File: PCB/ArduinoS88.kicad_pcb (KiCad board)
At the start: 2 copper layers, 49.5 x 61 mm, 24 parts, among them J1 S88 Output, J2 S88 Input, J3 AVR-ISP-6, J4 Screw_Terminal_01x03, J5 Screw_Terminal_01x03, J6 Screw_Terminal_01x03, J7 Screw_Terminal_01x03, J8 Screw_Terminal_01x03, J9 Screw_Terminal_01x02, U1 ATmega8-16PU

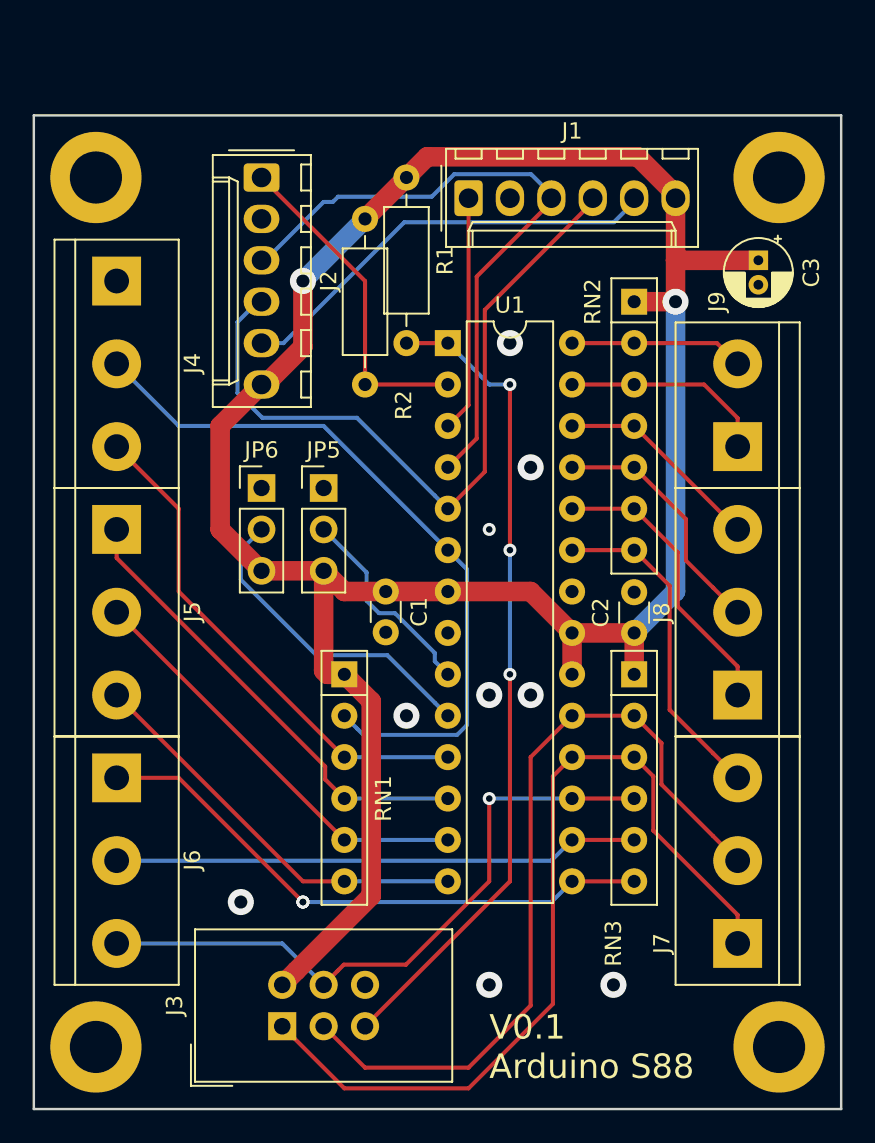
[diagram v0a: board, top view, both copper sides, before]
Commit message: Updated connectors and added Gerber files
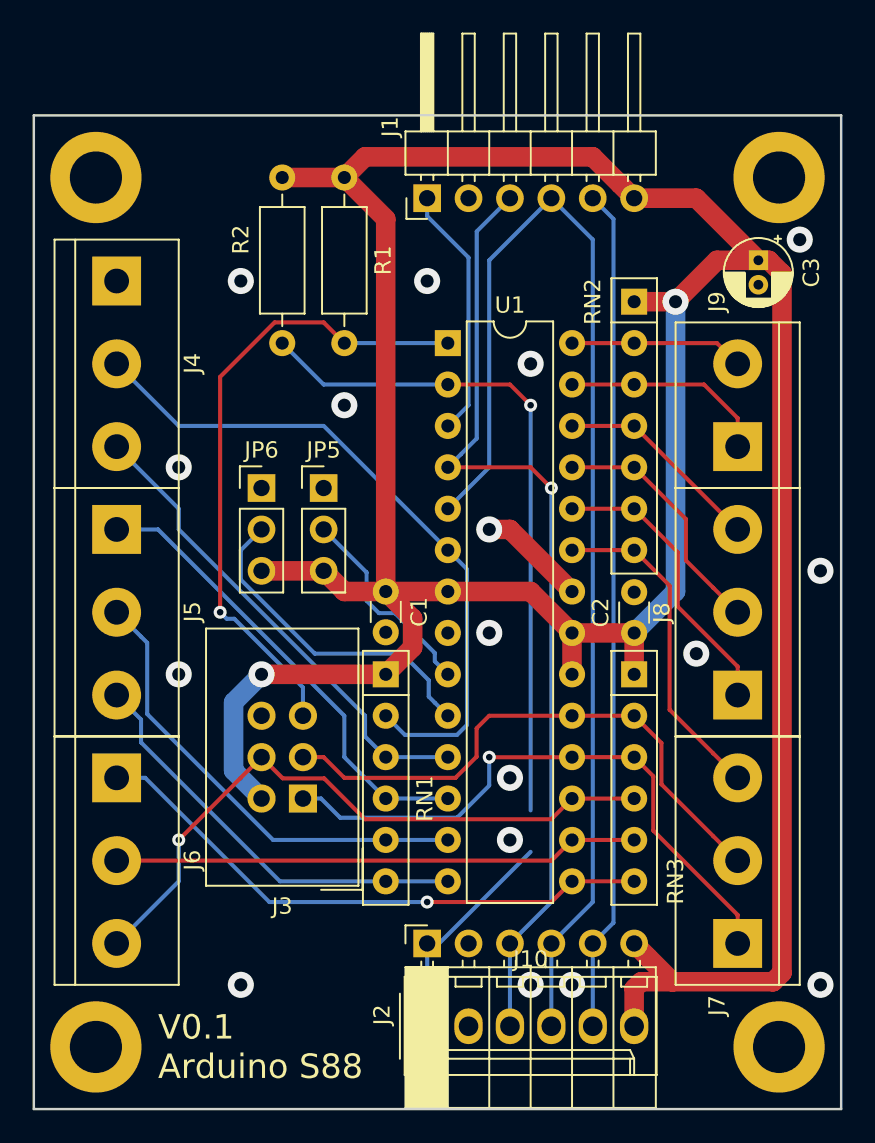
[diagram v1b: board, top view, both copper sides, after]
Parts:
- added J10: S88 Input, Connector_Molex:Molex_KK-254_AE-6410-06A_1x06_P2.54mm_Vertical, F.Cu at (94.0, 81.3)
- J1: footprint Connector_Molex:Molex_KK-254_AE-6410-06A_1x06_P2.54mm_Vertical -> Connector_PinHeader_2.54mm:PinHeader_1x06_P2.54mm_Horizontal
- J2: footprint Connector_Molex:Molex_KK-254_AE-6410-06A_1x06_P2.54mm_Vertical -> Connector_PinSocket_2.54mm:PinSocket_1x06_P2.54mm_Horizontal
- moved J2 48.1 mm to (94.0, 76.2), turned to 90 degrees
- moved J3 14.0 mm to (86.4, 67.3), turned to 180 degrees
- moved R2 5.68 mm to (85.1, 29.2)
- moved R1 3.81 mm to (88.9, 29.2)
- moved J1 2.54 mm to (94.0, 30.5), turned to 90 degrees
- moved RN1 2.54 mm to (91.4, 59.7)
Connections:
- net Net-(J1-Pad1) renamed /S88_DataOut
- net Net-(J1-Pad3) renamed /S88_CLK
- net Net-(J1-Pad4) renamed /S88_PS
- net Net-(J1-Pad5) renamed /S88_Reset
- net Net-(J2-Pad1) renamed /S88_DataIn
- net Net-(J3-Pad1) renamed /In8
- net Net-(J3-Pad3) renamed /In9
- net Net-(J3-Pad4) renamed /In7
- net Net-(J4-Pad2) renamed /In0
- net Net-(J4-Pad3) renamed /In1
- net Net-(J5-Pad1) renamed /In2
- net Net-(J5-Pad2) renamed /In3
- net Net-(J5-Pad3) renamed /In4
- net Net-(J6-Pad1) renamed /In5
- net Net-(J6-Pad2) renamed /In6
- net Net-(J7-Pad3) renamed /In10
- net Net-(J8-Pad1) renamed /In11
- net Net-(J8-Pad2) renamed /In12
- net Net-(J8-Pad3) renamed /In13
- net Net-(J9-Pad1) renamed /In14
- net Net-(J9-Pad2) renamed /In15
- net Net-(JP5-Pad2) renamed /Cfg0
- net Net-(JP6-Pad2) renamed /Cfg1
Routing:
- net VCC: track 142.6 -> 201.5 mm
- net /S88_DataIn: track 20.4 -> 55.4 mm, vias 0 -> 1
- net /S88_PS: track 44.9 -> 74.8 mm
- net /S88_Reset: track 26.9 -> 51.9 mm
- net /S88_CLK: track 39.9 -> 59.0 mm, vias 0 -> 1
- net /In8: track 53.8 -> 37.4 mm, vias 0 -> 1
- net /In9: track 49.5 -> 35.0 mm
- net Net-(J3-Pad5): track 50.5 -> 39.0 mm, vias 3 -> 1
- net GND: track 0.06 -> 6.71 mm, vias 8 -> 17
- net /In3: track 26.1 -> 28.7 mm
- net /In0: track 44.5 -> 42.0 mm
- net /In1: track 31.2 -> 29.7 mm
- net /S88_DataOut: track 14.5 -> 15.5 mm
- net /In4: track 25.1 -> 25.9 mm
- net /Cfg1: track 19.8 -> 20.4 mm
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
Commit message: Updated for manufacturing
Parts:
- moved REF** 1.27 mm to (114.3, 82.5)
- moved REF** 1.27 mm to (114.3, 29.2)
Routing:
- net VCC: track 201.5 -> 199.0 mm
- net GND: vias 17 -> 14
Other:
- board size 49.5 x 61 mm -> 48.3 x 61 mm
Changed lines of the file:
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@@
     (thickness 1.6)
     (drawings 8)
-    (tracks 232)
+    (tracks 229)
     (zones 0)
     (modules 25)
@@
     (pcbplotparams
       (layerselection 0x010f0_ffffffff)
-      (usegerberextensions false)
+      (usegerberextensions true)
       (usegerberattributes false)
       (usegerberadvancedattributes false)
@@
       (viasonmask false)
       (mode 1)
-      (useauxorigin false)
+      (useauxorigin true)
       (hpglpennumber 1)
       (hpglpenspeed 20)
@@
   )
   (module MountingHole:MountingHole_3.2mm_M3_DIN965_Pad (layer F.Cu)
-    (at 115.57 82.55)
+    (at 114.3 82.55)
     (descr "Mounting Hole 3.2mm, M3, DIN965")
     (tags "mounting hole 3.2mm m3 din965")
@@
   )
   (module MountingHole:MountingHole_3.2mm_M3_DIN965_Pad (layer F.Cu)
-    (at 115.57 29.21)
+    (at 114.3 29.21)
     (descr "Mounting Hole 3.2mm, M3, DIN965")
     (tags "mounting hole 3.2mm m3 din965")
@@
     (effects (font (size 1.5 1.5) (thickness 0.3)) (justify left))
   )
-  (target plus (at 69.85 86.36) (size 5) (width 0.15) (layer Edge.Cuts))
+  (target plus (at 87.022562 79.030951) (size 5) (width 0.15) (layer Edge.Cuts))
   (dimension 60.96 (width 0.3) (layer Dwgs.User)
     (gr_text "60,960 mm" (at 129.1 55.88 270) (layer Dwgs.User)
@@
   )
   (gr_line (start 69.85 86.36) (end 69.85 25.4) (layer Edge.Cuts) (width 0.15))
-  (gr_line (start 119.38 86.36) (end 69.85 86.36) (layer Edge.Cuts) (width 0.15))
-  (gr_line (start 119.38 25.4) (end 119.38 86.36) (layer Edge.Cuts) (width 0.15))
-  (gr_line (start 69.85 25.4) (end 119.38 25.4) (layer Edge.Cuts) (width 0.15))
-  (dimension 49.53 (width 0.3) (layer Dwgs.User)
-    (gr_text "49,530 mm" (at 94.691343 96.836647) (layer Dwgs.User)
+  (gr_line (start 118.11 86.36) (end 69.85 86.36) (layer Edge.Cuts) (width 0.15))
+  (gr_line (start 118.11 25.4) (end 118.11 86.36) (layer Edge.Cuts) (width 0.15))
+  (gr_line (start 69.85 25.4) (end 118.11 25.4) (layer Edge.Cuts) (width 0.15))
+  (dimension 48.26 (width 0.3) (layer Dwgs.User)
+    (gr_text "48,260 mm" (at 93.98 97.863353) (layer Dwgs.User)
       (effects (font (size 1.5 1.5) (thickness 0.3)))
     )
-    (feature1 (pts (xy 69.926343 88.386647) (xy 69.926343 95.323068)))
-    (feature2 (pts (xy 119.456343 88.386647) (xy 119.456343 95.323068)))
-    (crossbar (pts (xy 119.456343 94.736647) (xy 69.926343 94.736647)))
-    (arrow1a (pts (xy 69.926343 94.736647) (xy 71.052847 94.150226)))
-    (arrow1b (pts (xy 69.926343 94.736647) (xy 71.052847 95.323068)))
-    (arrow2a (pts (xy 119.456343 94.736647) (xy 118.329839 94.150226)))
-    (arrow2b (pts (xy 119.456343 94.736647) (xy 118.329839 95.323068)))
+    (feature1 (pts (xy 69.85 88.9) (xy 69.85 96.349774)))
+    (feature2 (pts (xy 118.11 88.9) (xy 118.11 96.349774)))
+    (crossbar (pts (xy 118.11 95.763353) (xy 69.85 95.763353)))
+    (arrow1a (pts (xy 69.85 95.763353) (xy 70.976504 95.176932)))
+    (arrow1b (pts (xy 69.85 95.763353) (xy 70.976504 96.349774)))
+    (arrow2a (pts (xy 118.11 95.763353) (xy 116.983496 95.176932)))
+    (arrow2b (pts (xy 118.11 95.763353) (xy 116.983496 96.349774)))
   )
   (via (at 78.74 46.99) (size 1.6) (drill 0.8) (layers F.Cu B.Cu) (net 3))
@@
   (segment (start 111.76 34.29) (end 109.22 36.83) (width 1.2) (layer F.Cu) (net 1))
   (segment (start 114.3 34.29) (end 111.76 34.29) (width 1.2) (layer F.Cu) (net 1))
-  (segment (start 110.49 30.48) (end 114.3 34.29) (width 1.2) (layer F.Cu) (net 1))
-  (segment (start 106.68 30.48) (end 110.49 30.48) (width 1.2) (layer F.Cu) (net 1))
   (segment (start 85.09 29.21) (end 88.9 29.21) (width 1.2) (layer F.Cu) (net 1))
   (segment (start 105.830001 29.630001) (end 106.68 30.48) (width 1.2) (layer F.Cu) (net 1))
@@
   (via (at 83.82 59.69) (size 1.6) (drill 0.8) (layers F.Cu B.Cu) (net 1))
   (segment (start 91.44 59.69) (end 83.82 59.69) (width 1.2) (layer F.Cu) (net 1))
+  (segment (start 107.95 30.48) (end 111.76 34.29) (width 1.2) (layer F.Cu) (net 1))
+  (segment (start 106.68 30.48) (end 107.95 30.48) (width 1.2) (layer F.Cu) (net 1))
   (segment (start 88.9 64.77) (end 88.9 64.77) (width 0.25) (layer B.Cu) (net 16))
   (segment (start 101.6 71.12) (end 74.93 71.12) (width 0.25) (layer F.Cu) (net 17))
@@
   (via (at 99.06 66.04) (size 1.6) (drill 0.8) (layers F.Cu B.Cu) (net 3))
   (via (at 99.06 69.85) (size 1.6) (drill 0.8) (layers F.Cu B.Cu) (net 3))
-  (via (at 116.84 33.02) (size 1.6) (drill 0.8) (layers F.Cu B.Cu) (net 3))
-  (via (at 118.11 53.34) (size 1.6) (drill 0.8) (layers F.Cu B.Cu) (net 3))
-  (via (at 118.11 78.74) (size 1.6) (drill 0.8) (layers F.Cu B.Cu) (net 3))
   (via (at 110.49 58.42) (size 1.6) (drill 0.8) (layers F.Cu B.Cu) (net 3))
   (via (at 100.33 78.74) (size 1.6) (drill 0.8) (layers F.Cu B.Cu) (net 3))
@@
     (polygon
       (pts
-        (xy 69.85 25.4) (xy 119.38 25.4) (xy 119.38 86.36) (xy 69.85 86.36)
+        (xy 69.85 25.4) (xy 118.11 25.4) (xy 118.11 86.36) (xy 69.85 86.36)
       )
     )
@@
     (polygon
       (pts
-        (xy 69.85 25.4) (xy 119.38 25.4) (xy 119.38 86.36) (xy 69.85 86.36)
+        (xy 69.85 25.4) (xy 118.11 25.4) (xy 118.11 86.36) (xy 69.85 86.36)
       )
     )

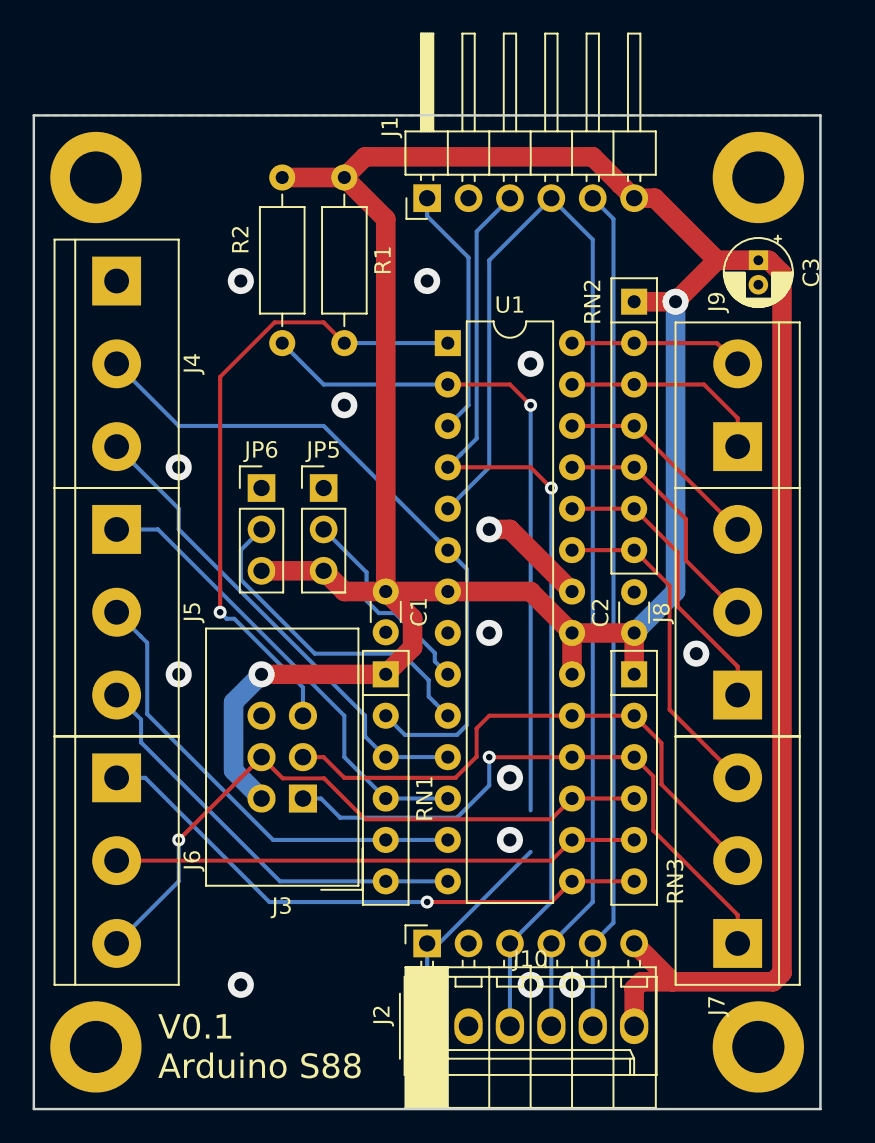
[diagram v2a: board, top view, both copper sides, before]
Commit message: Fix an unconnected trace. Bump PCB Version to v0.2.
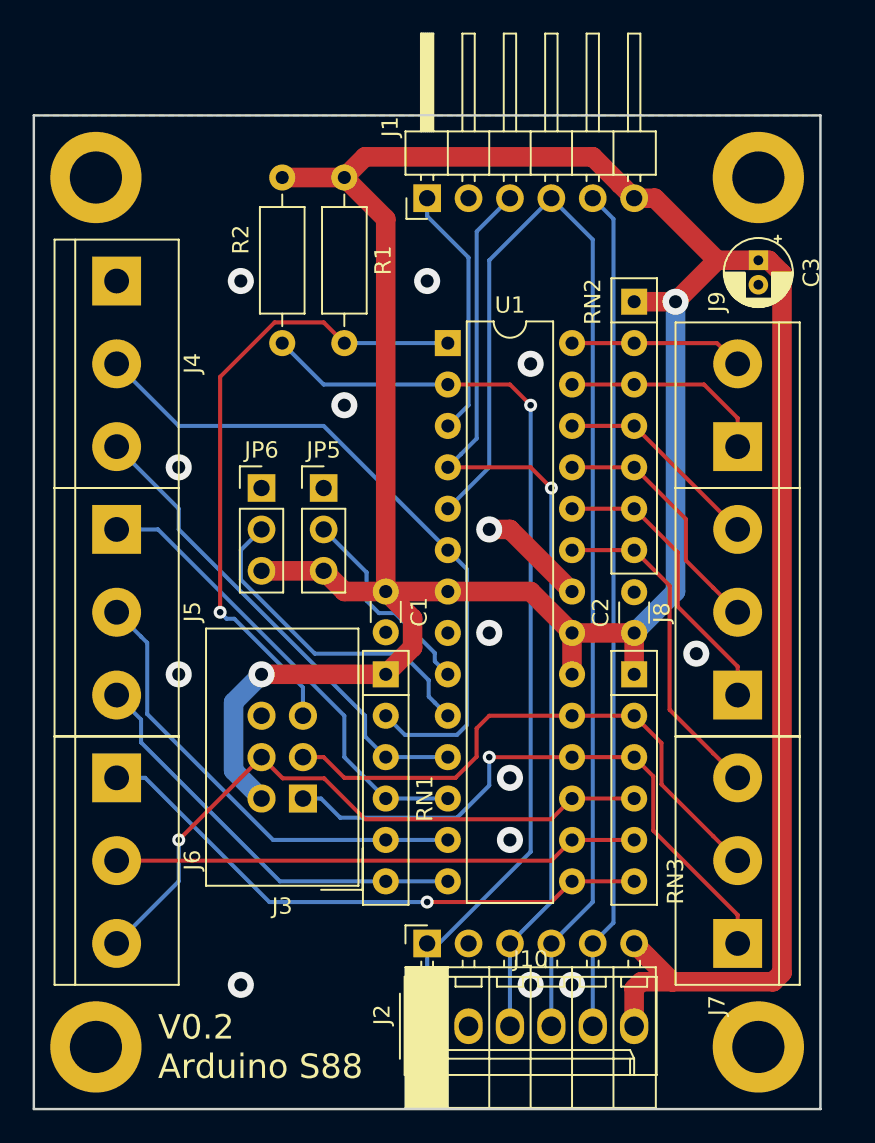
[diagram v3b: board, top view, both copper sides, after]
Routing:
- net /S88_DataIn: track 55.4 -> 58.0 mm
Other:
- board text added: "V0.2 Arduino S88"
- board text removed: "V0.1 Arduino S88"
